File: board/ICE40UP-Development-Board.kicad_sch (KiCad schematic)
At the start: 60 parts, among them X1 USB4105-GF-A, X2 Conn_01x17, X3 Conn_01x17, X4 Tag-Connect, Y1 48MHz

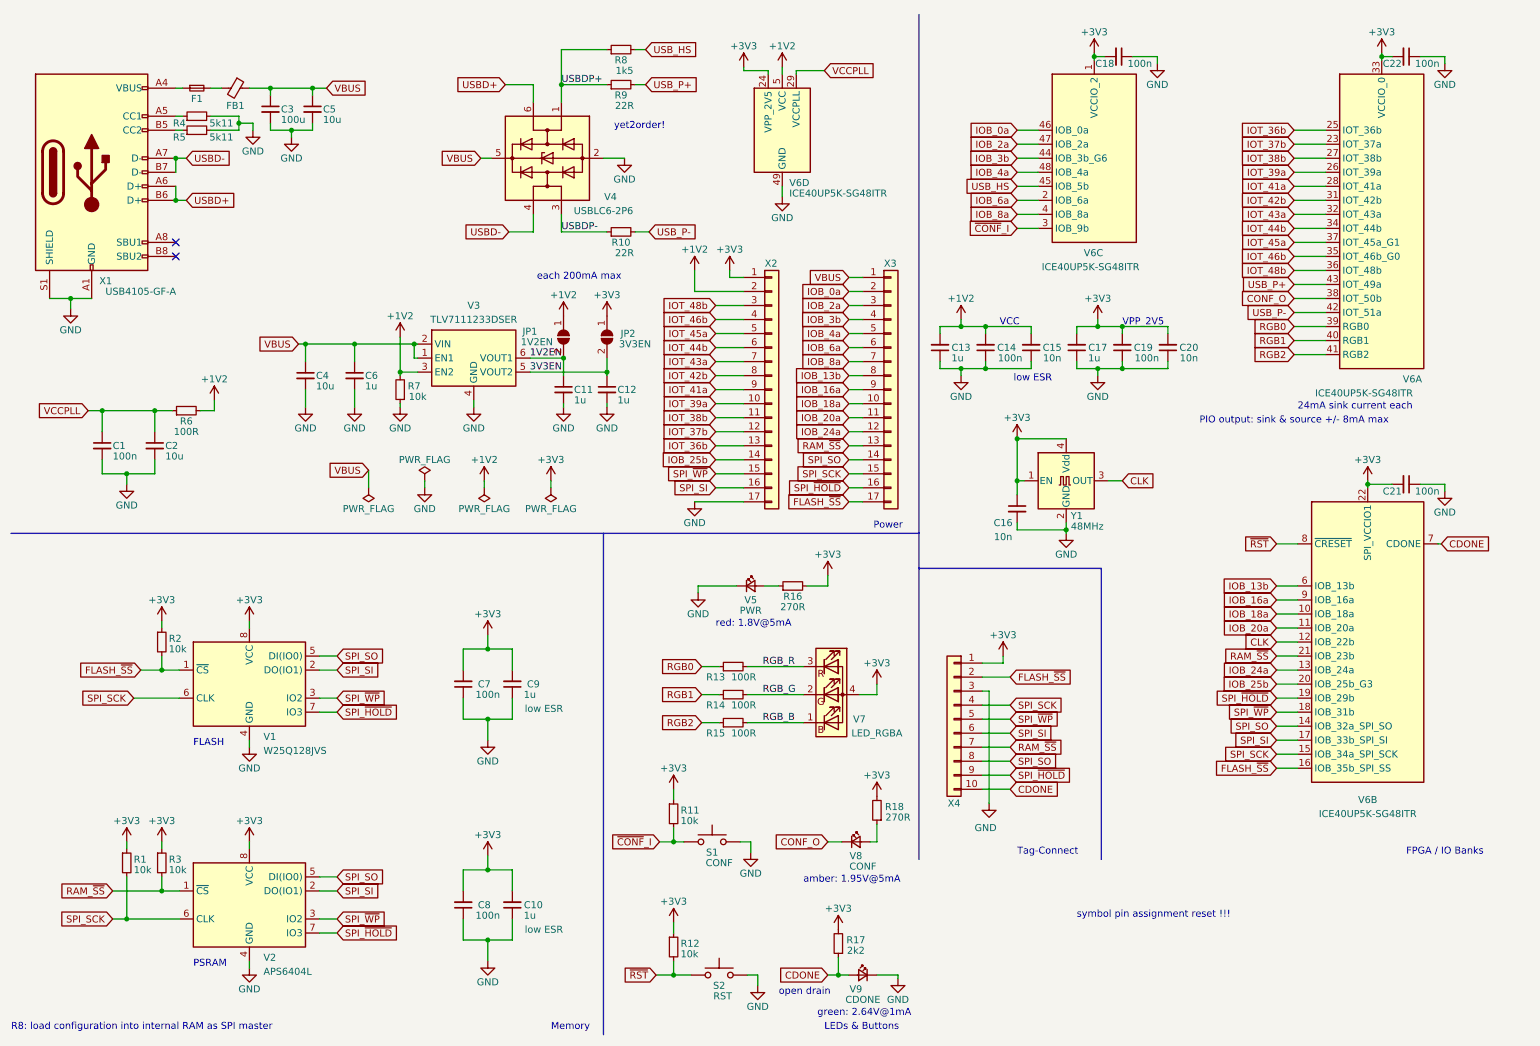
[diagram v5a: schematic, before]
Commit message: decrease pcb size; remove SPI-SS signals from breakout pins
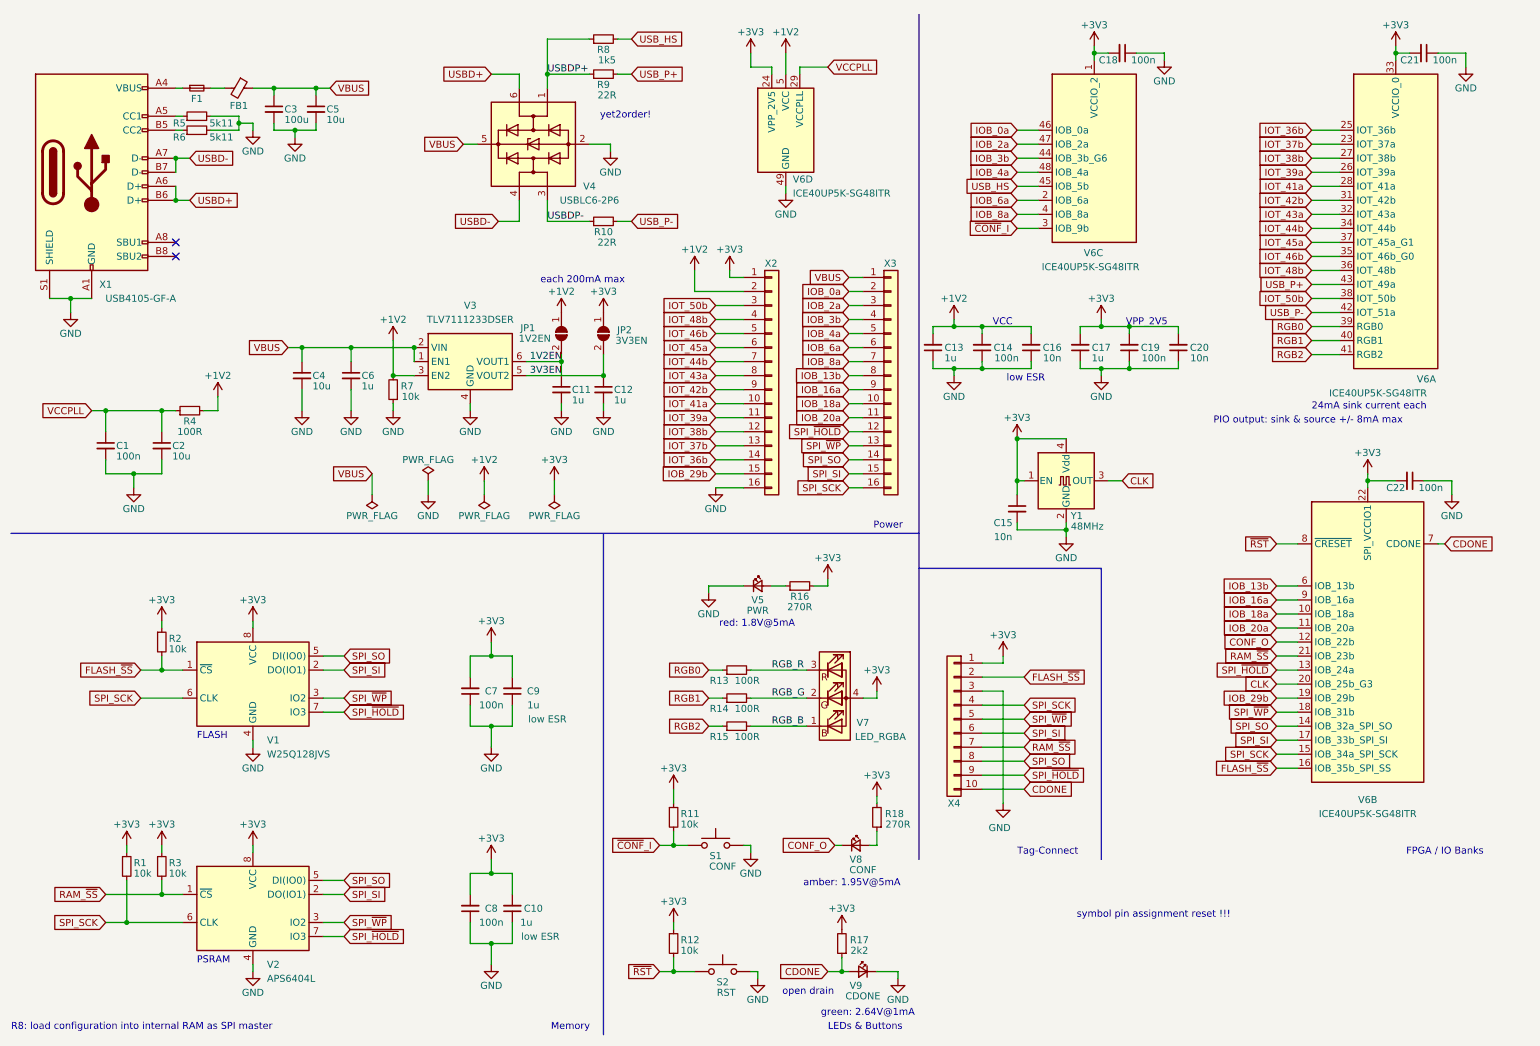
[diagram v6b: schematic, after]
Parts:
- removed X2, X3: Conn_01x17, Connector_PinHeader_2.54mm:PinHeader_1x17_P2.54mm_Vertical, symbol Connector_Generic:Conn_01x17
- added X2, X3: Conn_01x16, Connector_PinHeader_2.54mm:PinHeader_1x16_P2.54mm_Vertical, symbol Connector_Generic:Conn_01x16
- renumbered C16 to C15, C15 to C16, C22 to C21, C21 to C22, R6 to R4, R4 to R5, R5 to R6
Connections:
- net IOB_24a is gone; now on net SPI_~{HOLD}: V6.13 (IOB_24a)
- net IOB_25b is gone; now on net CLK: V6.20 (IOB_25b_G3)
- net +1V2: now also X2.2 (Pin_2)
- net +3V3: now also X2.1 (Pin_1)
- net CLK: no longer V6.12 (IOB_22b)
- net CONF_O: now also V6.12 (IOB_22b); no longer V6.38 (IOT_50b)
- net GND: now also X2.16 (Pin_16); no longer V3.9 (GND)
- net IOB_0a: now also X3.2 (Pin_2)
- net IOB_13b: now also X3.8 (Pin_8)
- net IOB_16a: now also X3.9 (Pin_9)
- net IOB_18a: now also X3.10 (Pin_10)
- net IOB_20a: now also X3.11 (Pin_11)
- net IOB_2a: now also X3.3 (Pin_3)
- net IOB_3b: now also X3.4 (Pin_4)
- net IOB_4a: now also X3.5 (Pin_5)
- net IOB_6a: now also X3.6 (Pin_6)
- net IOB_8a: now also X3.7 (Pin_7)
- net IOT_36b: now also X2.14 (Pin_14)
- net IOT_37b: now also X2.13 (Pin_13)
- net IOT_38b: now also X2.12 (Pin_12)
- net IOT_39a: now also X2.11 (Pin_11)
- net IOT_41a: now also X2.10 (Pin_10)
- net IOT_42b: now also X2.9 (Pin_9)
- net IOT_43a: now also X2.8 (Pin_8)
- net IOT_44b: now also X2.7 (Pin_7)
- net IOT_45a: now also X2.6 (Pin_6)
- net IOT_46b: now also X2.5 (Pin_5)
- net IOT_48b: now also X2.4 (Pin_4)
- net SPI_SCK: now also X3.16 (Pin_16)
- net SPI_SI: now also X3.15 (Pin_15)
- net SPI_SO: now also X3.14 (Pin_14)
- net SPI_~{HOLD}: now also X3.12 (Pin_12); no longer V6.19 (IOB_29b)
- net SPI_~{WP}: now also X3.13 (Pin_13)
- net VBUS: now also X3.1 (Pin_1)
- new net IOB_29b: V6.19 (IOB_29b), X2.15 (Pin_15)
- new net IOT_50b: V6.38 (IOT_50b), X2.3 (Pin_3)
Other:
- moved on the sheet: C1, C10, C12, C13, C14, C17, C18, C19, C2, C20, C21, C22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

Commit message: change led resistor values
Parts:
- R16, R18: value 270R -> 10k
- R17: value 2k2 -> 10k
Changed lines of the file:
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@@
       (effects (font (size 1.27 1.27)))
     )
-    (property "Value" "270R" (at 172.72 160.02 0)
+    (property "Value" "10k" (at 172.72 160.02 0)
       (effects (font (size 1.27 1.27)))
     )
@@
       (effects (font (size 1.27 1.27)))
     )
-    (property "Value" "270R" (at 154.94 120.65 90)
+    (property "Value" "10k" (at 154.94 120.65 90)
       (effects (font (size 1.27 1.27)))
     )
@@
       (effects (font (size 1.27 1.27)))
     )
-    (property "Value" "2k2" (at 165.735 182.88 0)
-      (effects (font (size 1.27 1.27)))
-    )
+    (property "Value" "10k" (at 165.735 182.88 0)
+      (effects (font (size 1.27 1.27)))
+    )

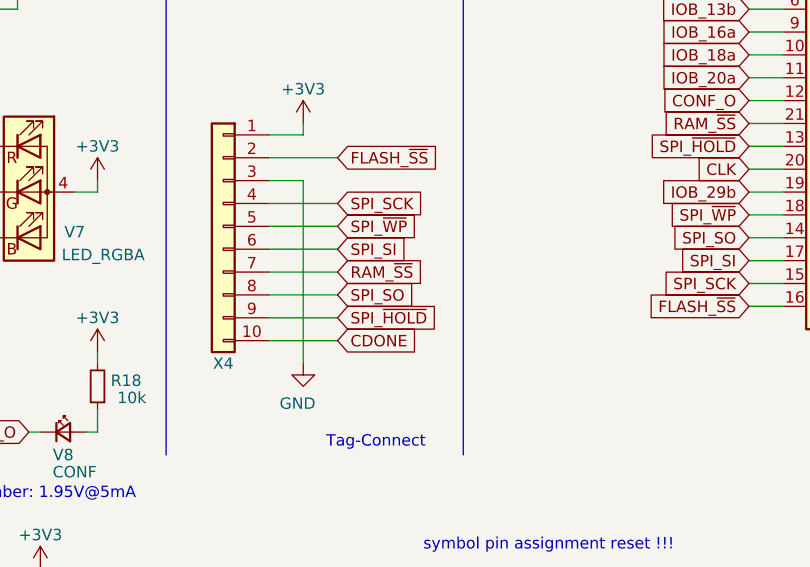
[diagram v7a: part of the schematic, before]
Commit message: change tag-connect pinout; add reset signal to tag-connect
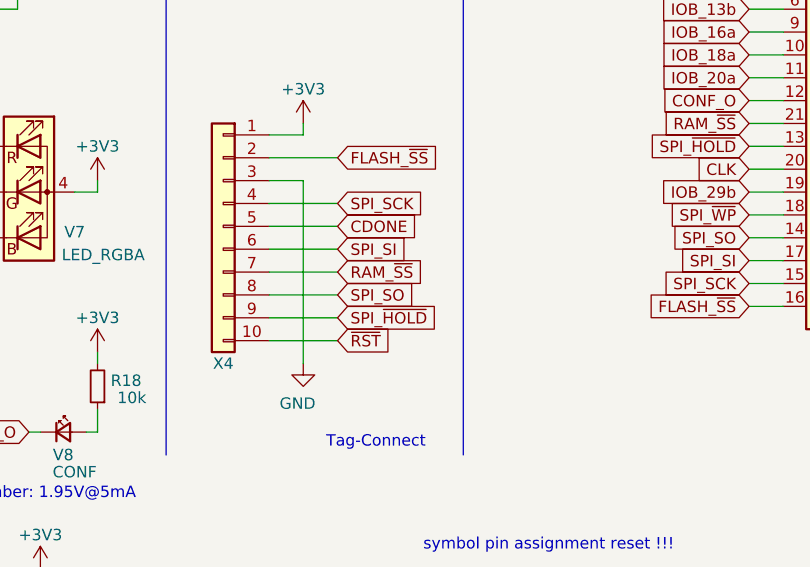
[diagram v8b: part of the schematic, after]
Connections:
- net CDONE: now also X4.5 (Pin_5); no longer X4.10 (Pin_10)
- net SPI_~{WP}: no longer X4.5 (Pin_5)
- net ~{RST}: now also X4.10 (Pin_10)
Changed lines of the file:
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@@
     )
   )
-  (global_label "CDONE" (shape input) (at 195.58 153.67 0) (fields_autoplaced)
-    (effects (font (size 1.27 1.27)) (justify left))
-    (property "Intersheetrefs" "${INTERSHEET_REFS}" (at 204.3431 153.5906 0)
+  (global_label "CDONE" (shape input) (at 195.58 140.97 0) (fields_autoplaced)
+    (effects (font (size 1.27 1.27)) (justify left))
+    (property "Intersheetrefs" "${INTERSHEET_REFS}" (at 204.3431 140.8906 0)
       (effects (font (size 1.27 1.27)) (justify left) hide)
     )
@@
     )
   )
-  (global_label "SPI_~{WP}" (shape input) (at 195.58 140.97 0) (fields_autoplaced)
-    (effects (font (size 1.27 1.27)) (justify left))
-    (property "Intersheetrefs" "${INTERSHEET_REFS}" (at 204.7664 140.8906 0)
-      (effects (font (size 1.27 1.27)) (justify left) hide)
-    )
-  )
   (global_label "SPI_~{HOLD}" (shape input) (at 163.83 88.9 180) (fields_autoplaced)
     (effects (font (size 1.27 1.27)) (justify right))
@@
     )
   )
+  (global_label "~{RST}" (shape input) (at 195.58 153.67 0) (fields_autoplaced)
+    (effects (font (size 1.27 1.27)) (justify left))
+    (property "Intersheetrefs" "${INTERSHEET_REFS}" (at 201.4402 153.5906 0)
+      (effects (font (size 1.27 1.27)) (justify left) hide)
+    )
+  )
